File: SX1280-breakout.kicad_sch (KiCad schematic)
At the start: 34 parts, among them J17 Conn_Coaxial, X1 52.000 MHz

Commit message: switched to 0.4mm castellations & routed
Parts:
- C1: value (none) -> 100nF; footprint (none) -> Capacitor_SMD:C_0402_1005Metric
- C2: value (none) -> 1nF; footprint (none) -> Capacitor_SMD:C_0402_1005Metric
- C3, C4: value (none) -> 10nF; footprint (none) -> Capacitor_SMD:C_0402_1005Metric
- C5, C7: value (none) -> 0.1uF; footprint (none) -> Capacitor_SMD:C_0402_1005Metric
- C6: value (none) -> 470nF; footprint (none) -> Capacitor_SMD:C_0402_1005Metric
- J1, J10, J11, J12, J13, J14, J15, J16, J2, J3, J4, J5, J6, J7, J8, J9: value (none) -> Conn_01x01; footprint (none) -> custom-footprints:castellated_04mm
- J17: value Conn_Coaxial -> W.FL-R-SMT-1(10)
- L1: value (none) -> 15uH; footprint (none) -> Inductor_SMD:L_0805_2012Metric
- R1, R2, R3, R4, R5: value (none) -> 1k; footprint (none) -> Resistor_SMD:R_0402_1005Metric
- U1: value (none) -> SX1280IMLTRT; footprint (none) -> custom-footprints:QFN50P400X400X80-25N-D
- U2: value (none) -> 2450FM07D0034T; footprint (none) -> custom-footprints:2450FM07D0034T
- X1: symbol SX1280-breakout-rescue:XLH536025_000000I-dk_Oscillators -> symbols:NT2016SA; Height (none) -> 0.8; Manufacturer_Name (none) -> NIHON DEMPA KOGYO; Manufacturer_Part_Number (none) -> NT2016SA-38.4MHZ-END4679A
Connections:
- net +3V3: now also X1.4 (VCC)
- net GND: now also X1.1 (VCONT), X1.2 (GND)
- net at C2.2: now also X1.3 (OUTPUT)
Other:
- note added: "50ohm 2.4 GHz"
- note added: "w.FL MHF III AMMC"
- note removed: "50ohm 0.6mm 2-layer FR4 2.4 GHz"
- company: RExLab Stanford University -> (none)
- moved on the sheet: C1

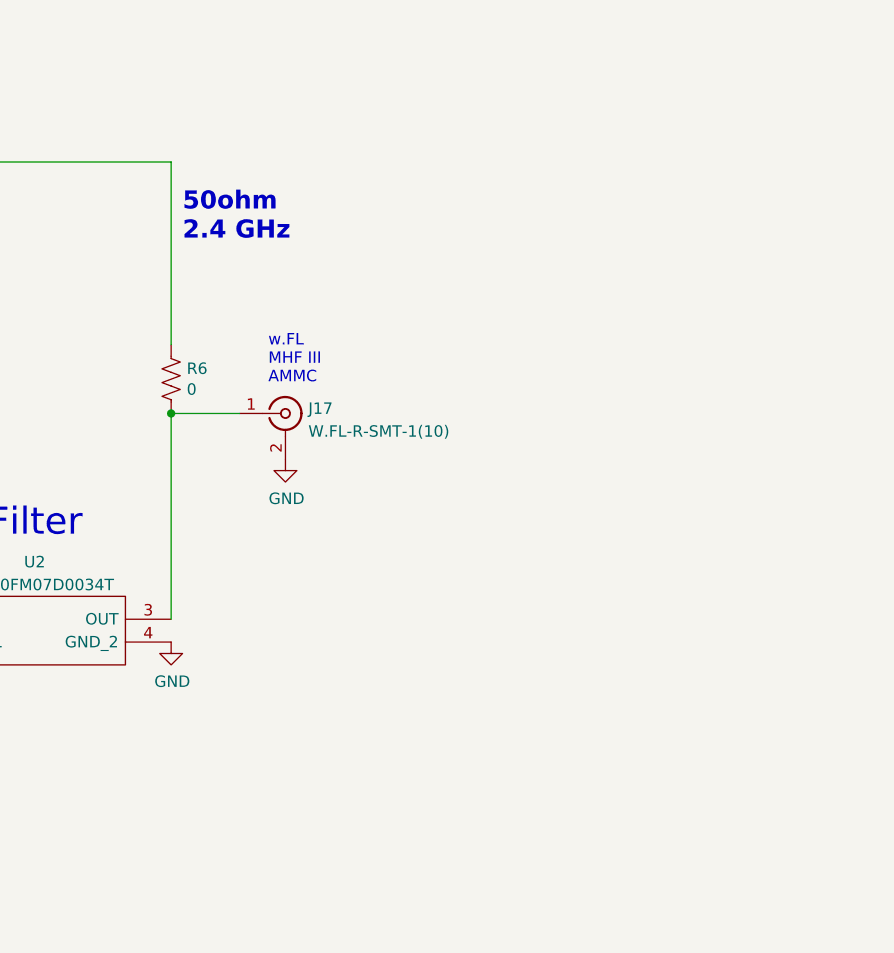
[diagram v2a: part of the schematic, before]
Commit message: changed to u.FL (undecided)
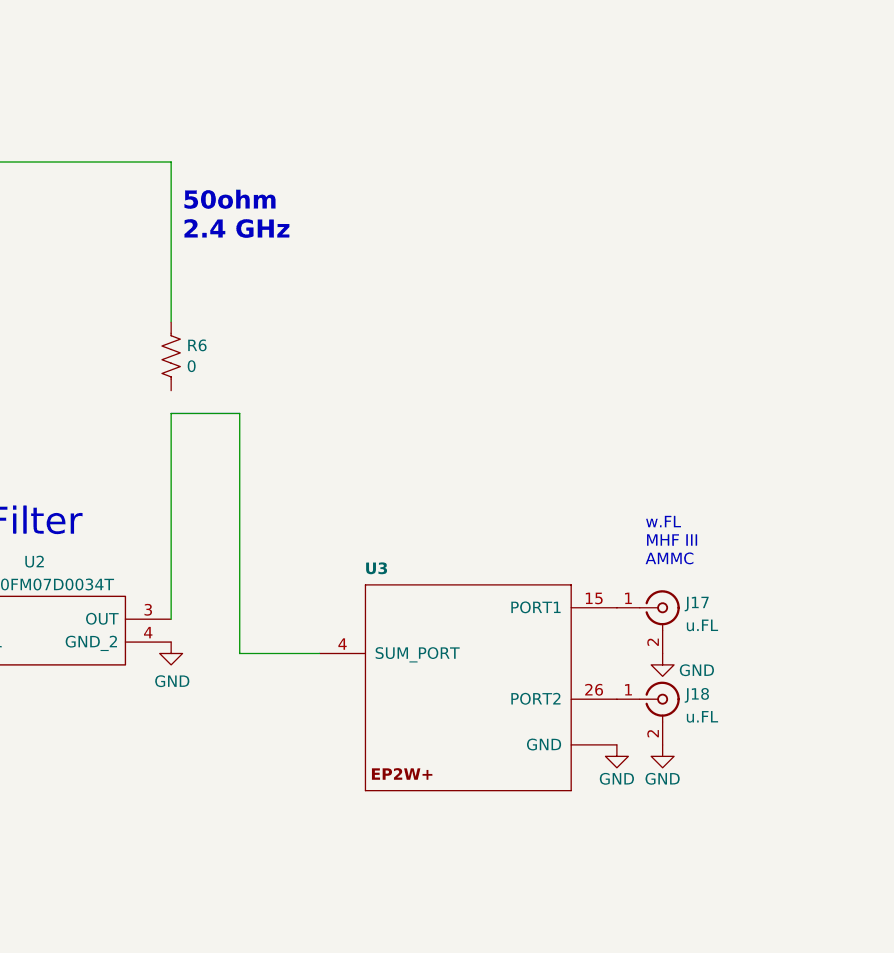
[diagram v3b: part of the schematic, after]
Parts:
- added J18: u.FL, Connector_Coaxial:U.FL_Hirose_U.FL-R-SMT-1_Vertical, symbol Connector:Conn_Coaxial
- added U3: EP2W+, custom-footprints:QFN32-5X5MM, symbol mainboard:EP2W+
- J17: value W.FL-R-SMT-1(10) -> u.FL; footprint custom-footprints:w.FL -> Connector_Coaxial:U.FL_Hirose_U.FL-R-SMT-1_Vertical
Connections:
- net GND: now also J18.2 (Ext), U3.1 (GND), U3.10 (GND), U3.11 (GND), U3.12 (GND), U3.13 (GND), U3.14 (GND), U3.16 (GND), U3.17 (GND), U3.18 (GND), U3.19 (GND), U3.2 (GND), U3.20 (GND), U3.21 (GND), U3.22 (GND), U3.23 (GND), U3.24 (GND), U3.25 (GND), U3.27 (GND), U3.28 (GND), U3.29 (GND), U3.3 (GND), U3.30 (GND), U3.31 (GND), U3.32 (GND), U3.5 (GND), U3.6 (GND), U3.7 (GND), U3.8 (GND), U3.9 (GND), U3.EP (GND)
- new net: U2.3 (OUT), U3.4 (SUM_PORT)
- new net: J18.1 (In), U3.26 (PORT2)
- new net: J17.1 (In), U3.15 (PORT1)
- now unconnected: R6.1
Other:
- moved on the sheet: J17, R6
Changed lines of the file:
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@@
     (comment 2 "M.Holliday")
-  )
-  (junction (at 203.2 80.01) (diameter 0) (color 0 0 0 0)
   )
   (junction (at 56.515 116.84) (diameter 0) (color 0 0 0 0)
@@
   (no_connect (at 149.86 39.37))
   (no_connect (at 109.22 120.65))
+  (wire (pts (xy 210.82 106.68) (xy 219.71 106.68))
+    (stroke (width 0) (type default) (color 0 0 0 0))
+  )
   (wire (pts (xy 157.48 107.95) (xy 160.02 107.95))
     (stroke (width 0) (type default) (color 0 0 0 0))
@@
     (stroke (width 0) (type default) (color 0 0 0 0))
   )
+  (wire (pts (xy 203.2 69.85) (xy 203.2 52.07))
+    (stroke (width 0) (type default) (color 0 0 0 0))
+  )
   (wire (pts (xy 110.49 46.99) (xy 107.95 46.99))
     (stroke (width 0) (type default) (color 0 0 0 0))
@@
     (stroke (width 0) (type default) (color 0 0 0 0))
   )
-  (wire (pts (xy 203.2 72.39) (xy 203.2 52.07))
-    (stroke (width 0) (type default) (color 0 0 0 0))
-  )
   (wire (pts (xy 166.37 128.27) (xy 166.37 130.81))
     (stroke (width 0) (type default) (color 0 0 0 0))
@@
   )
   (wire (pts (xy 149.86 102.87) (xy 172.72 102.87))
+    (stroke (width 0) (type default) (color 0 0 0 0))
+  )
+  (wire (pts (xy 210.82 80.01) (xy 210.82 106.68))
     (stroke (width 0) (type default) (color 0 0 0 0))
   )
@@
     (effects (font (size 3.9878 3.9878) (thickness 0.7976) bold) (justify left bottom))
   )
-  (text "w.FL\nMHF III\nAMMC" (at 213.995 76.835 0)
+  (text "w.FL\nMHF III\nAMMC" (at 255.905 97.155 0)
     (effects (font (size 1.27 1.27)) (justify left bottom))
   )
@@
     (pin "1")
   )
-  (symbol (lib_id "Device:R_US") (at 203.2 76.2 180) (unit 1)
-    (in_bom yes) (on_board yes)
-    (property "Reference" "R6" (id 0) (at 204.9272 75.0316 0)
+  (symbol (lib_id "Device:R_US") (at 203.2 73.66 180) (unit 1)
+    (in_bom yes) (on_board yes)
+    (property "Reference" "R6" (id 0) (at 204.9272 72.4916 0)
       (effects (font (size 1.27 1.27)) (justify right))
     )
-    (property "Value" "0" (id 1) (at 204.9272 77.343 0)
+    (property "Value" "0" (id 1) (at 204.9272 74.803 0)
       (effects (font (size 1.27 1.27)) (justify right))
     )
-    (property "Footprint" "Resistor_SMD:R_0201_0603Metric" (id 2) (at 202.184 75.946 90)
-      (effects (font (size 1.27 1.27)) hide)
-    )
-    (property "Datasheet" "~" (id 3) (at 203.2 76.2 0)
-      (effects (font (size 1.27 1.27)) hide)
-    )
-    (pin "1")
-    (pin "2")
-  )
-  (symbol (lib_id "power:GND") (at 215.9 85.09 0) (unit 1)
-    (in_bom yes) (on_board yes)
-    (property "Reference" "#PWR0107" (id 0) (at 215.9 91.44 0)
-      (effects (font (size 1.27 1.27)) hide)
-    )
-    (property "Value" "GND" (id 1) (at 216.027 89.4842 0))
-    (property "Footprint" "" (id 2) (at 215.9 85.09 0)
-      (effects (font (size 1.27 1.27)) hide)
-    )
-    (property "Datasheet" "" (id 3) (at 215.9 85.09 0)
-      (effects (font (size 1.27 1.27)) hide)
-    )
-    (pin "1")
-  )
-  (symbol (lib_id "Connector:Conn_Coaxial") (at 215.9 80.01 0) (unit 1)
+    (property "Footprint" "Resistor_SMD:R_0201_0603Metric" (id 2) (at 202.184 73.406 90)
+      (effects (font (size 1.27 1.27)) hide)
+    )
+    (property "Datasheet" "~" (id 3) (at 203.2 73.66 0)
+      (effects (font (size 1.27 1.27)) hide)
+    )
+    (pin "1")
+    (pin "2")
+  )
+  (symbol (lib_id "power:GND") (at 257.81 106.68 0) (unit 1)
+    (in_bom yes) (on_board yes)
+    (property "Reference" "#PWR0107" (id 0) (at 257.81 113.03 0)
+      (effects (font (size 1.27 1.27)) hide)
+    )
+    (property "Value" "GND" (id 1) (at 261.62 108.585 0))
+    (property "Footprint" "" (id 2) (at 257.81 106.68 0)
+      (effects (font (size 1.27 1.27)) hide)
+    )
+    (property "Datasheet" "" (id 3) (at 257.81 106.68 0)
+      (effects (font (size 1.27 1.27)) hide)
+    )
+    (pin "1")
+  )
+  (symbol (lib_id "Connector:Conn_Coaxial") (at 257.81 111.76 0) (unit 1)
     (in_bom yes) (on_board yes) (fields_autoplaced)
-    (property "Reference" "J17" (id 0) (at 218.4401 79.4685 0)
-      (effects (font (size 1.27 1.27)) (justify left))
-    )
-    (property "Value" "W.FL-R-SMT-1(10)" (id 1) (at 218.4401 82.0054 0)
-      (effects (font (size 1.27 1.27)) (justify left))
-    )
-    (property "Footprint" "custom-footprints:w.FL" (id 2) (at 215.9 80.01 0)
-      (effects (font (size 1.27 1.27)) hide)
-    )
-    (property "Datasheet" " ~" (id 3) (at 215.9 80.01 0)
-      (effects (font (size 1.27 1.27)) hide)
-    )
-    (pin "1")
-    (pin "2")
+    (property "Reference" "J18" (id 0) (at 260.3501 111.2185 0)
+      (effects (font (size 1.27 1.27)) (justify left))
+    )
+    (property "Value" "u.FL" (id 1) (at 260.3501 113.7554 0)
+      (effects (font (size 1.27 1.27)) (justify left))
+    )
+    (property "Footprint" "Connector_Coaxial:U.FL_Hirose_U.FL-R-SMT-1_Vertical" (id 2) (at 257.81 111.76 0)
+      (effects (font (size 1.27 1.27)) hide)
+    )
+    (property "Datasheet" " ~" (id 3) (at 257.81 111.76 0)
+      (effects (font (size 1.27 1.27)) hide)
+    )
+    (pin "1")
+    (pin "2")
+  )
+  (symbol (lib_id "power:GND") (at 257.81 116.84 0) (unit 1)
+    (in_bom yes) (on_board yes)
+    (property "Reference" "#PWR0109" (id 0) (at 257.81 123.19 0)
+      (effects (font (size 1.27 1.27)) hide)
+    )
+    (property "Value" "GND" (id 1) (at 257.81 120.65 0))
+    (property "Footprint" "" (id 2) (at 257.81 116.84 0)
+      (effects (font (size 1.27 1.27)) hide)
+    )
+    (property "Datasheet" "" (id 3) (at 257.81 116.84 0)
+      (effects (font (size 1.27 1.27)) hide)
+    )
+    (pin "1")
+  )
+  (symbol (lib_id "Connector:Conn_Coaxial") (at 257.81 101.6 0) (unit 1)
+    (in_bom yes) (on_board yes) (fields_autoplaced)
+    (property "Reference" "J17" (id 0) (at 260.3501 101.0585 0)
+      (effects (font (size 1.27 1.27)) (justify left))
+    )
+    (property "Value" "u.FL" (id 1) (at 260.3501 103.5954 0)
+      (effects (font (size 1.27 1.27)) (justify left))
+    )
+    (property "Footprint" "Connector_Coaxial:U.FL_Hirose_U.FL-R-SMT-1_Vertical" (id 2) (at 257.81 101.6 0)
+      (effects (font (size 1.27 1.27)) hide)
+    )
+    (property "Datasheet" " ~" (id 3) (at 257.81 101.6 0)
+      (effects (font (size 1.27 1.27)) hide)
+    )
+    (pin "1")
+    (pin "2")
+  )
+  (symbol (lib_id "power:GND") (at 252.73 116.84 0) (unit 1)
+    (in_bom yes) (on_board yes)
+    (property "Reference" "#PWR0108" (id 0) (at 252.73 123.19 0)
+      (effects (font (size 1.27 1.27)) hide)
+    )
+    (property "Value" "GND" (id 1) (at 252.73 120.65 0))
+    (property "Footprint" "" (id 2) (at 252.73 116.84 0)
+      (effects (font (size 1.27 1.27)) hide)
+    )
+    (property "Datasheet" "" (id 3) (at 252.73 116.84 0)
+      (effects (font (size 1.27 1.27)) hide)
+    )
+    (pin "1")
+  )
+  (symbol (lib_id "mainboard:EP2W+") (at 237.49 106.68 0) (unit 1)
+    (in_bom yes) (on_board yes)
+    (property "Reference" "U3" (id 0) (at 227.33 96.52 0)
+      (effects (font (size 1.27 1.27) bold) (justify right top))
+    )
+    (property "Value" "EP2W+" (id 1) (at 237.49 106.68 0)
+      (effects (font (size 1.27 1.27)) hide)
+    )
+    (property "Footprint" "custom-footprints:QFN32-5X5MM" (id 2) (at 237.49 106.68 0)
+      (effects (font (size 1.27 1.27)) hide)
+    )
+    (property "Datasheet" "https://www.minicircuits.com/pdfs/EP2W+.pdf" (id 3) (at 237.49 106.68 0)
+      (effects (font (size 1.27 1.27)) hide)
+    )
+    (property "Description" "RF Splitter DC-Pass" (id 5) (at 237.49 106.68 0)
+      (effects (font (size 1.27 1.27)) hide)
+    )
+    (property "Flight" "EP2W+" (id 6) (at 237.49 106.68 0)
+      (effects (font (size 1.27 1.27)) hide)
+    )
+    (property "Manufacturer_Name" "Mini Circuits" (id 7) (at 237.49 106.68 0)
+      (effects (font (size 1.27 1.27)) hide)
+    )
+    (property "Manufacturer_Part_Number" "EP2W+" (id 8) (at 237.49 106.68 0)
+      (effects (font (size 1.27 1.27)) hide)
+    )
+    (pin "1")
+    (pin "10")
+    (pin "11")
+    (pin "12")
+    (pin "13")
+    (pin "14")
+    (pin "15")
+    (pin "16")
+    (pin "17")
+    (pin "18")
+    (pin "19")
+    (pin "2")
+    (pin "20")
+    (pin "21")
+    (pin "22")
+    (pin "23")
+    (pin "24")
+    (pin "25")
+    (pin "26")
+    (pin "27")
+    (pin "28")
+    (pin "29")
+    (pin "3")
+    (pin "30")
+    (pin "31")
+    (pin "32")
+    (pin "4")
+    (pin "5")
+    (pin "6")
+    (pin "7")
+    (pin "8")
+    (pin "9")
+    (pin "EP")
   )
   (sheet_instances
@@
       (reference "#PWR0107") (unit 1) (value "GND") (footprint "")
     )
+    (path "/8cf544d3-5d2f-402c-bf39-04d87279bdea"
+      (reference "#PWR0108") (unit 1) (value "GND") (footprint "")
+    )
+    (path "/33e15a5b-9c50-478f-bd5b-f828403b32a3"
+      (reference "#PWR0109") (unit 1) (value "GND") (footprint "")
+    )
     (path "/00000000-0000-0000-0000-00005d611e57"
       (reference "C1") (unit 1) (value "100nF") (footprint "Capacitor_SMD:C_0402_1005Metric")
@@
     )
     (path "/42a2d086-ca5c-483c-b9b4-96b240bd2bb0"
-      (reference "J17") (unit 1) (value "W.FL-R-SMT-1(10)") (footprint "custom-footprints:w.FL")
+      (reference "J17") (unit 1) (value "u.FL") (footprint "Connector_Coaxial:U.FL_Hirose_U.FL-R-SMT-1_Vertical")
+    )
+    (path "/144e921c-09f9-4e46-8904-db378eb2dd88"
+      (reference "J18") (unit 1) (value "u.FL") (footprint "Connector_Coaxial:U.FL_Hirose_U.FL-R-SMT-1_Vertical")
     )
     (path "/00000000-0000-0000-0000-00005d18add6"
@@
       (reference "U2") (unit 1) (value "2450FM07D0034T") (footprint "custom-footprints:2450FM07D0034T")
     )
+    (path "/e88eff66-38b6-4df2-a4c3-c0cb54f3031b"
+      (reference "U3") (unit 1) (value "EP2W+") (footprint "custom-footprints:QFN32-5X5MM")
+    )
     (path "/00000000-0000-0000-0000-00005d18c449"
